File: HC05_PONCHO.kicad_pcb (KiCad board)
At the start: 2 copper layers, 34 parts, among them J1 MOUNT_HOLE, J2 MOUNT_HOLE, J3 BARREL_JACK, Q1 Q_NPN_EBC, SW1 SW_SPDT, SW2 SW_Push, SW3 SW_Push, U1 LD1117S33CTR, U2 MOUDLE-BLUETOOTH-HC-05(34P-27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, U3 HMC5883L

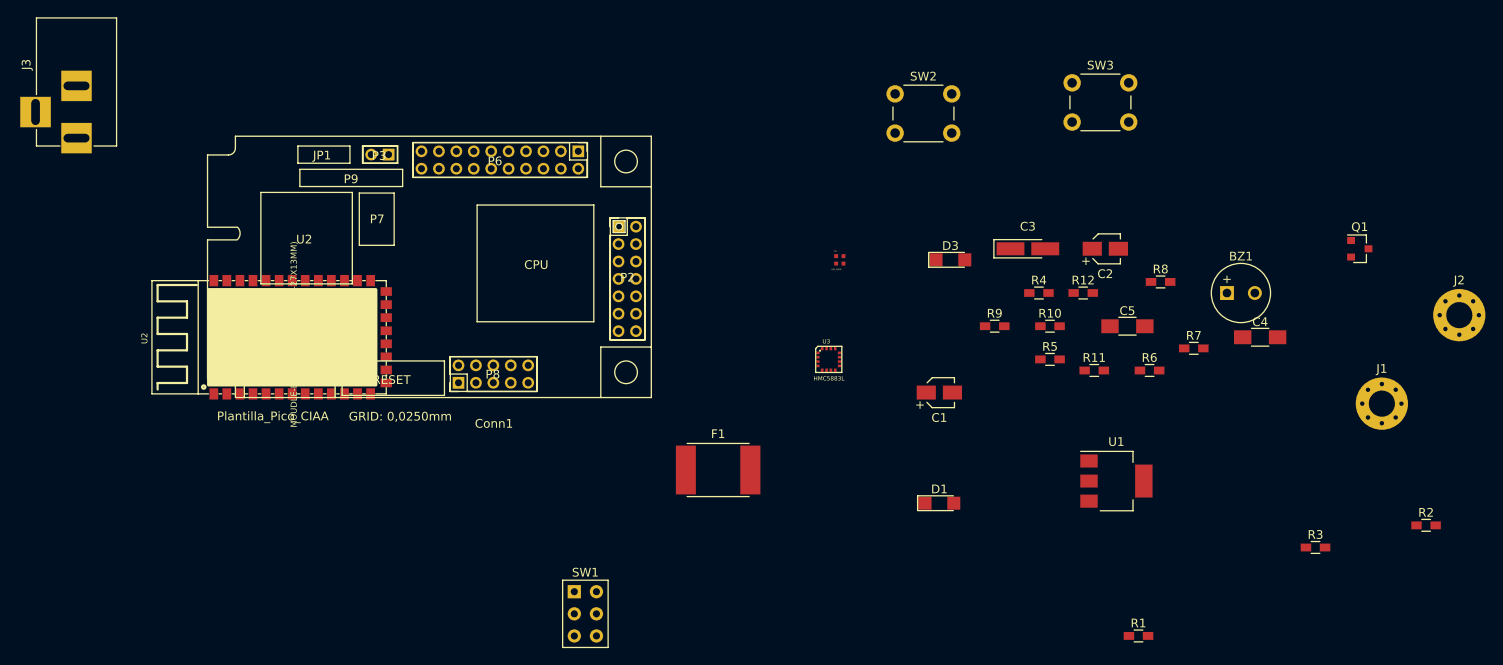
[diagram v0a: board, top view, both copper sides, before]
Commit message: Esquematico V1.1
Correccion parcial de las observaciones realizadas por el revisor, se reflejan el archivo de revision ubicado en la carpeta doc
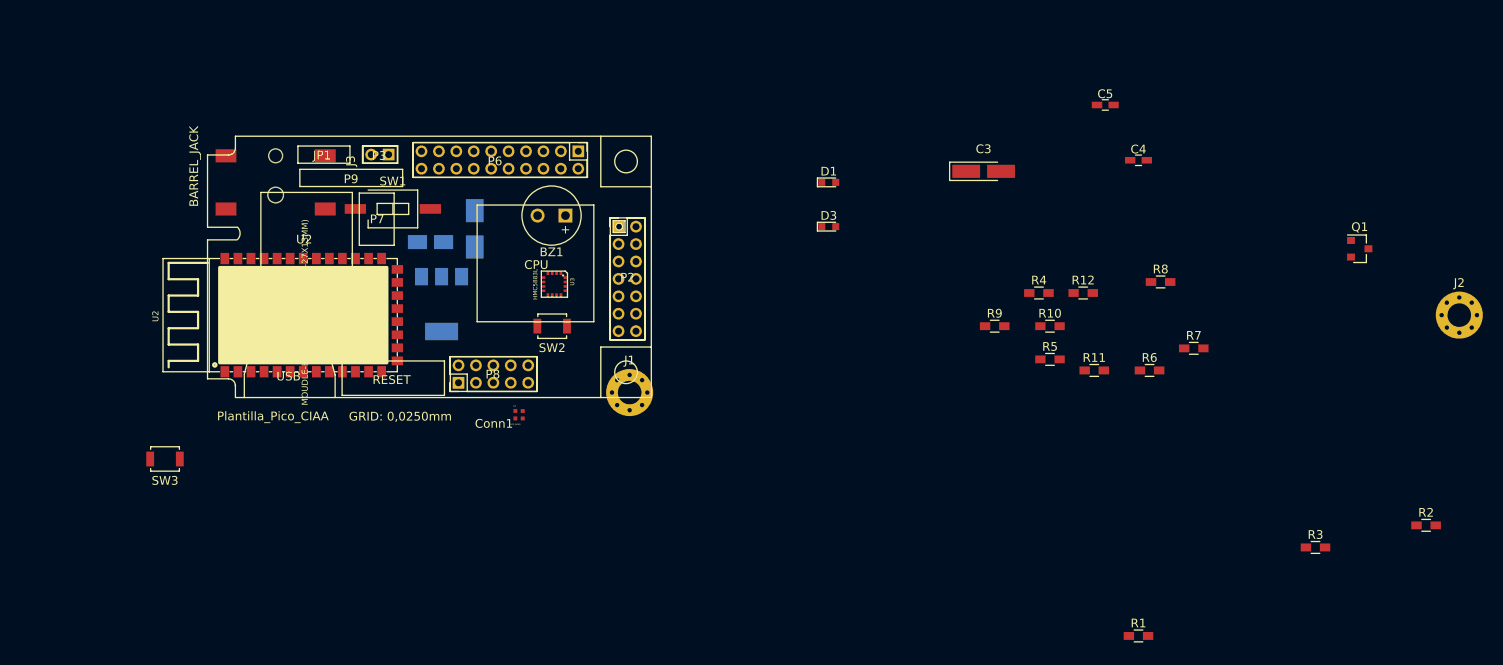
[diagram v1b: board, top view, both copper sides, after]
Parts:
- C1, C2, U1: moved to B.Cu
- C4, C5: footprint Capacitors_SMD:C_1206_HandSoldering -> Capacitors_SMD:C_0603_HandSoldering
- D1, D3: footprint LEDs:LED_1206 -> LEDs:LED_0603
- F1: footprint Fuse_Holders_and_Fuses:Fuse_SMD2920 -> Fuse_Holders_and_Fuses:Fuse_SMD1206_HandSoldering; moved to B.Cu
- J1, J2: footprint Mounting_Holes:MountingHole_3mm_Pad_Via -> Mounting_Holes:MountingHole_2.7mm_Pad_Via
- J3: footprint Connectors:BARREL_JACK -> PJ-002AH-SMT-TR:CUI_PJ-002AH-SMT-TR
- SW1: footprint Buttons_Switches_THT:SW_NKK_G1xJP -> Buttons_Switches_SMD:SW_DIP_x1_W8.61mm_Slide_LowProfile
- SW2, SW3: footprint Buttons_Switches_THT:SW_PUSH_6mm -> Buttons_Switches_SMD:SW_SPST_B3U-1000P
- moved SW3 112.7 mm to (39.4, 120.7), turned to 180 degrees
- moved J1 86.4 mm to (92.7, 113.0)
- moved U1 80.1 mm to (71.1, 102.9), turned to 270 degrees
- moved C2 77.5 mm to (69.8, 95.8), turned to 180 degrees
- moved BZ1 76.5 mm to (85.3, 92.7), turned to 180 degrees
- moved C1 65.3 mm to (64.0, 101.3), turned to 90 degrees
- moved SW1 48.6 mm to (65.5, 91.9)
- moved SW2 47.6 mm to (83.8, 105.4), turned to 180 degrees
- moved D2 40.9 mm to (80.0, 115.6)
- moved F1 39.3 mm to (74.9, 94.2), turned to 270 degrees
- moved D1 39.0 mm to (115.6, 88.9)
- moved U3 32.7 mm to (84.1, 100.6), turned to 270 degrees
- moved C5 25.5 mm to (147.3, 80.0)
- moved C4 24.7 mm to (151.1, 86.4)
- moved J3 23.4 mm to (52.1, 88.9)
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
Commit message: Avance para segunda revision.
Se realizan todos los cambios solicitados por el docente y el corrector, ademas se continua con el avance hasta el placement del PCB
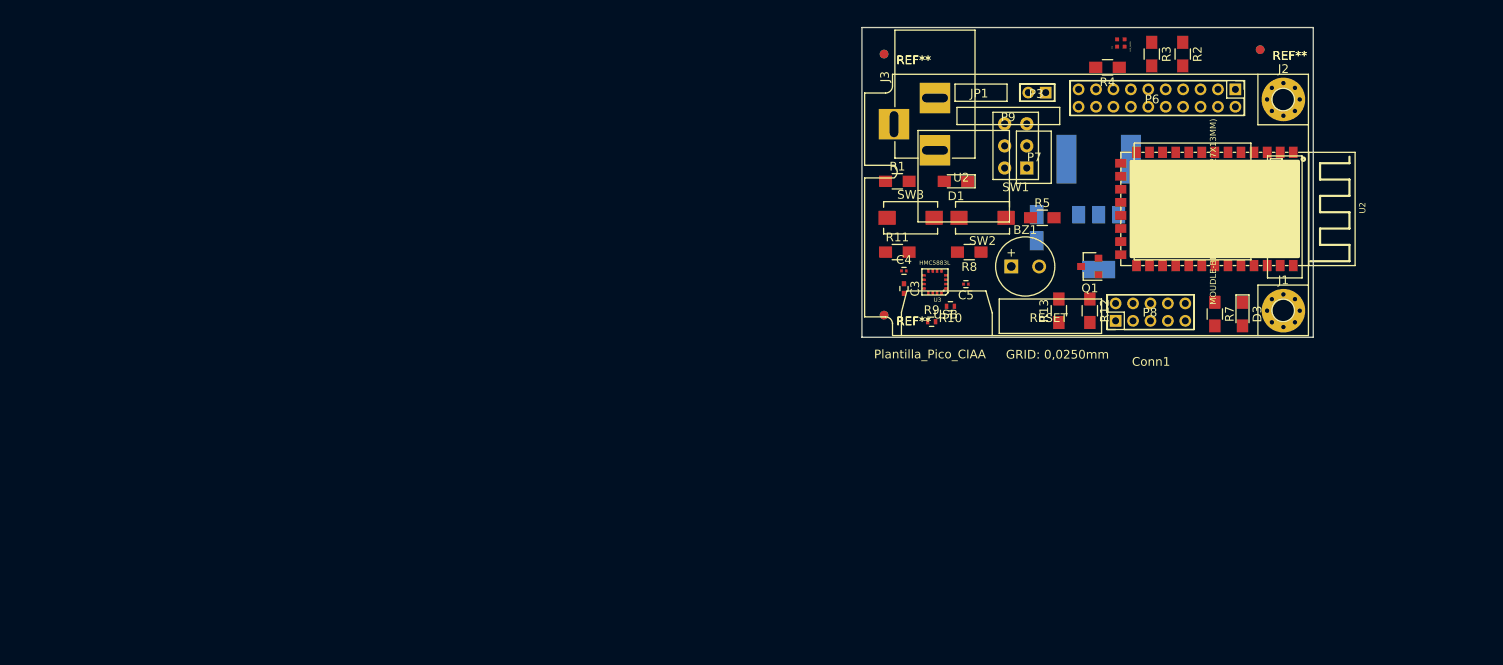
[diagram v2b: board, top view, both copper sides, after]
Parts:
- added R13: 470, Resistors_SMD:R_0805_HandSoldering, F.Cu at (142.0, 103.6)
- added REF**: Fiducial_1mm_Dia_2.54mm_Outer_CopperBottom, Fiducials:Fiducial_1mm_Dia_2.54mm_Outer_CopperBottom, F.Cu at (165.1, 73.7)
- added REF**: Fiducial_1mm_Dia_2.54mm_Outer_CopperTop, Fiducials:Fiducial_1mm_Dia_2.54mm_Outer_CopperTop, F.Cu at (121.9, 74.2)
- added REF**: Fiducial_1mm_Dia_2.54mm_Outer_CopperTop, Fiducials:Fiducial_1mm_Dia_2.54mm_Outer_CopperTop, F.Cu at (165.1, 73.7)
- added REF**: Fiducial_1mm_Dia_2.54mm_Outer_CopperTop, Fiducials:Fiducial_1mm_Dia_2.54mm_Outer_CopperTop, F.Cu at (121.9, 104.1)
- added REF**: Fiducial_1mm_Dia_2.54mm_Outer_CopperBottom, Fiducials:Fiducial_1mm_Dia_2.54mm_Outer_CopperBottom, F.Cu at (121.9, 74.2)
- added REF**: Fiducial_1mm_Dia_2.54mm_Outer_CopperBottom, Fiducials:Fiducial_1mm_Dia_2.54mm_Outer_CopperBottom, F.Cu at (121.9, 104.1)
- C3: footprint Capacitors_Tantalum_SMD:CP_Tantalum_Case-A_EIA-3216-18_Hand -> Capacitors_SMD:C_0402
- C4, C5: footprint Capacitors_SMD:C_0603_HandSoldering -> Capacitors_SMD:C_0201
- D1: value LED -> LED/RED; footprint LEDs:LED_0603 -> LEDs:LED_0805_HandSoldering
- D3: value LED -> LED/BLUE; footprint LEDs:LED_0603 -> LEDs:LED_0805_HandSoldering
- F1: footprint Fuse_Holders_and_Fuses:Fuse_SMD1206_HandSoldering -> Fuse_Holders_and_Fuses:Fuse_SMD2920
- J1, J2: footprint Mounting_Holes:MountingHole_2.7mm_Pad_Via -> Mounting_Holes:MountingHole_2.5mm_Pad_Via
- J3: footprint PJ-002AH-SMT-TR:CUI_PJ-002AH-SMT-TR -> Connectors:BARREL_JACK
- R1, R11, R12, R2, R3, R4, R5, R7, R8: footprint Resistors_SMD:R_0603_HandSoldering -> Resistors_SMD:R_0805_HandSoldering
- R10, R9: footprint Resistors_SMD:R_0603_HandSoldering -> Resistors_SMD:R_0402
- R6: footprint Resistors_SMD:R_0603_HandSoldering -> Resistors_SMD:R_0805_HandSoldering; moved to B.Cu
- SW1: footprint Buttons_Switches_SMD:SW_DIP_x1_W8.61mm_Slide_LowProfile -> Buttons_Switches_THT:SW_NKK_G1xJP
- SW2, SW3: footprint Buttons_Switches_SMD:SW_SPST_B3U-1000P -> Buttons_Switches_SMD:SW_SPST_EVQPE1
- moved SW3 90.0 mm to (125.0, 93.0), turned to 0 degrees
- moved U2 83.9 mm to (149.1, 91.9), turned to 270 degrees
- moved C2 83.8 mm to (153.7, 94.1), turned to 270 degrees
- moved D2 81.2 mm to (149.1, 72.9), turned to 90 degrees
- moved C1 75.8 mm to (139.4, 94.1)
- moved J3 75.8 mm to (127.8, 85.2)
- moved Conn1 75.8 mm to (166.9, 86.9)
- moved Plantilla_Pico_CIAA 75.8 mm to (166.9, 86.9)
- moved U1 75.8 mm to (146.6, 95.8)
- moved J1 75.6 mm to (167.8, 103.6)
- moved SW1 72.9 mm to (138.3, 87.2), turned to 180 degrees
- moved F1 72.1 mm to (146.6, 86.2), turned to 0 degrees
- moved R2 60.9 mm to (156.2, 74.2), turned to 270 degrees
- moved R3 59.7 mm to (152.7, 74.2), turned to 270 degrees
- moved R1 59.1 mm to (123.4, 88.8)
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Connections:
- Conn1 pad 42: (no net) -> Net-(Conn1-Pad42)
- Conn1 pad 43: Net-(Conn1-Pad43) -> HC05-RST
- R10 pad 2: Net-(Conn1-Pad41) -> Net-(Conn1-Pad39)
- R12 pad 2: Net-(Conn1-Pad39) -> Net-(Conn1-Pad41)
- R6 pad 2: Net-(Conn1-Pad40) -> Net-(Conn1-Pad44)
- R9 pad 2: Net-(Conn1-Pad44) -> Net-(Conn1-Pad42)
- U2 pad 11: Net-(U2-Pad11) -> HC05-RST
- U2 pad 3: Net-(U2-Pad3) -> Net-(Conn1-Pad17)
- U2 pad 4: Net-(U2-Pad4) -> Net-(Conn1-Pad18)
- U2 pad 5: Net-(U2-Pad5) -> Net-(Conn1-Pad20)
- U3 pad 1: Net-(Conn1-Pad41) -> Net-(Conn1-Pad39)
- U3 pad 16: Net-(Conn1-Pad44) -> Net-(Conn1-Pad42)
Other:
- board outline added: 51.8 x 35.6 mm

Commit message: Revision de carpetas
Limpieza de documentos que ya no se utilizaban en el proyecto.
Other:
- board text added: "Grillas - Posicionamiento: 10,00 mils y 5 mils - Ruteo: Valores mínimos - Pista: - Vía: - Orificio Vía: Capas - Top: Si - Bottom: Si Terminación superficial:"
